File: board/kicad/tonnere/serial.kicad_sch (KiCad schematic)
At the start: 1 part, among them J14 STM USART TTL

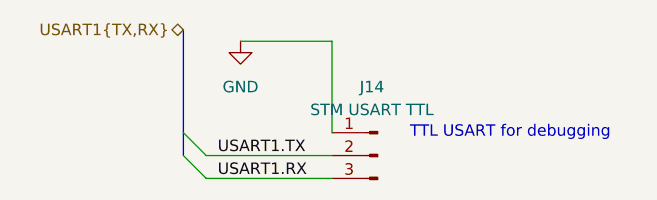
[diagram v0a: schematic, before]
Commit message: Changed video dac to 5 bit R2R and 6th-8th bits as pattern and/or sigma delta.
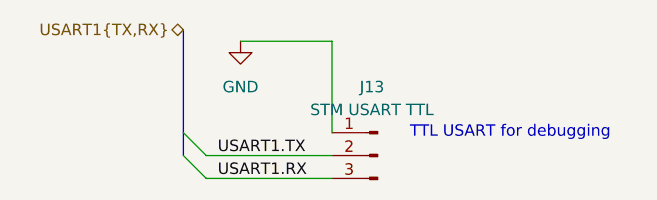
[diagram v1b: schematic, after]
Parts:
- renumbered J14 to J13
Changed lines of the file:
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@@
 		(in_pos_files yes)
 		(dnp no)
-		(property "Reference" "J14"
+		(property "Reference" "J13"
 			(at 73.025 33.02 0)
 			(show_name no)
@@
 			(project "tonnere"
 				(path "/eb8e239c-f2ec-4b57-8f5c-6c75d6b59ab3/ffed6702-cf67-401e-a39f-b369f1396c7d"
-					(reference "J14")
+					(reference "J13")
 					(unit 1)
 				)
